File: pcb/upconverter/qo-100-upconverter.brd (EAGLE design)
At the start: 85 x 60 mm, 170 parts, among them CON1 2EDG-2P, Q1 AO3400, Q2 AO3401, U1 EFM32PG1B200F256GM32, U10 MIC23155, U11 LT8636, U12 ADP3334, U13 LT8636, U14 ADP150UJZ-3.3, U15 ADP150UJZ-3.3, U2 DSB321SDA, U3 ADF4351, U4 HMC8073, U5 MAX2671, U6 2450BP15E0100, U7 ADL5601, U8 ADL5601, U9 ADPA9002

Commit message: Lots of changes PCBs in production Stencil in production Added and changed simulation files
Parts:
- added C90: 10uF, Capacitor:CAP1206
- C27: value 10uF -> 100nF
- C28: value 100nF -> 10uF
- C29: value 100pF -> 100nF
- C30: value 47pF -> 100pF
- C32: value 220pF -> 47pF
- C33: value DNP -> 220pF
- C34, C49: value 12pF -> DNP
- C35: value 100uF -> 12pF; device Capacitor:CAP1206 -> Capacitor:CAP0603
- C36: value 1uF -> 100uF; device Capacitor:CAP0603 -> Capacitor:CAP1206
- C37, C41: value 1nF -> 1uF
- C38, C42: value 15pF -> 1nF
- C39, C43: value 12pF -> 15pF
- C40: value 1uF -> 12pF
- C44: value 0 Ohms -> 12pF
- C45: value 12pF -> 0 Ohms
- C46: value 22uF -> 12pF; device Capacitor:CAP1206 -> Capacitor:CAP0603
- C47: value 1nF -> 22uF; device Capacitor:CAP0603 -> Capacitor:CAP1206
- C48: value DNP -> 1nF
- C50: value DNP -> 12pF
- C53: value 1nF -> DNP
- C54: value 100nF -> 1nF
- C55: value 4.7uF -> 100nF
- C57: value 470pF -> 4.7uF
- C58, C60, C78: value 1uF -> 470pF
- C59, C77: value 470pF -> 1uF
- C62, C79: value 10nF -> 1uF
- C63: value 470pF -> 10nF
- C64: value 100nF -> 470pF
- C66, C81: value 10pF -> 100nF
- C67: value 470pF -> 10pF
- C68: value 100uF -> 470pF; device Capacitor:CAP1206 -> Capacitor:CAP0603
- C70: value 100nF -> 100uF; device Capacitor:CAP0603 -> Capacitor:CAP1206
- C71, C76: value 1uF -> 100nF
- C72: value 4.7uF -> 1uF
- C73: value 22uF -> 4.7uF; device Capacitor:CAP1206 -> Capacitor:CAP0603
- C74, C85: value 1uF -> 22uF; device Capacitor:CAP0603 -> Capacitor:CAP1206
- C75: value 100nF -> 1uF
- C80: value 100nF -> 10nF
- C82: value 1uF -> 10pF
- C84, C87: value 22uF -> 1uF; device Capacitor:CAP1206 -> Capacitor:CAP0603
- C88: value 100nF -> 22uF; device Capacitor:CAP0603 -> Capacitor:CAP1206
- C89: value 10uF -> 100nF; device Capacitor:CAP1206 -> Capacitor:CAP0603
- U4: value HMC8073 -> F1951NBGI; device Analog Devices:LFCSP16 -> Renesas:QFN24
- moved C82 42.1 mm to (7.00, 24.7), turned to 0 degrees
- moved C54 37.8 mm to (16.4, 44.5), turned to 270 degrees
- moved C67 31.4 mm to (21.6, 2.50), turned to 0 degrees
- moved C63 29.4 mm to (21.6, 7.90)
- moved C72 28.1 mm to (41.7, 39.1), turned to 270 degrees
- moved C78 27.1 mm to (33.6, 39.1), turned to 270 degrees
- moved C85 25.1 mm to (30.3, 31.5), turned to 0 degrees
- moved C87 24.2 mm to (51.7, 40.1), turned to 270 degrees
- moved C71 22.8 mm to (34.3, 17.5), turned to 90 degrees
- moved C77 22.2 mm to (17.3, 24.1), turned to 0 degrees
- moved C58 22.1 mm to (50.7, 10.6), turned to 180 degrees
- moved C60 21.8 mm to (43.2, 16.2), turned to 90 degrees
- moved C55 20.1 mm to (41.4, 16.2), turned to 90 degrees
- moved C59 19.0 mm to (30.1, 2.50), turned to 0 degrees
- moved C56 18.8 mm to (26.7, 2.50), turned to 180 degrees
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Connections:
- removed net ATT_LE: R10.2, U1.24, U4.12
- new net !ATT_CS: R10.2, U1.24, U4.9
- new net N$28: C27.1, U4.2
- net 12V0: now also C82.1, C85.1, C89.1; no longer C81.1, C84.1, C87.1
- net 12V0_ANA_PA_CLEAN: now also C47.1, C74.1, C76.1; no longer C45.1, C73.1, C75.1
- net 12V0_BST: now also C81.2; no longer C80.2
- net 12V0_FB: now also C82.2; no longer C81.2
- net 12V0_INTVCC: now also C79.1; no longer C78.1
- net 12V0_SS: now also C80.1; no longer C79.1
- net 12V0_SW: now also C81.1; no longer C80.1
- net 12V0_VSENSE: now also C64.1; no longer C63.1
- net 3V3: now also C65.1, C69.1; no longer C64.1, C68.1
- net 3V3_ANA_MIXER_CLEAN: now also C29.1, C32.1, C86.1, U4.14; no longer C27.1, C30.1, C85.1, U4.1
- net 3V3_ANA_PLL_CLEAN: now also C87.1; no longer C86.1
- net 3V3_SOFTSTART: now also C60.1; no longer C59.1
- net 5V0: now also C55.1, C57.1, C67.1, C72.1, C84.1; no longer C54.1, C56.1, C66.1, C69.1, C82.1
- net 5V0_ANA_PA_CLEAN: now also C39.1, C43.1, C78.1; no longer C35.1, C40.1, C77.1
- net 5V0_BST: now also C66.2; no longer C65.2
- net 5V0_FB: now also C67.2; no longer C66.2
- net 5V0_INTVCC: now also C62.1; no longer C61.1
- net 5V0_SS: now also C63.1; no longer C62.1
- net 5V0_SW: now also C66.1; no longer C65.1
- net 5V0_VSENSE: now also C68.1; no longer C67.1
- net GND: now also C32.2, C34.2, C39.2, C43.2, C49.2, C65.2, C77.2, C80.2, C90.2, U4.19, U4.20, U4.21, U4.22, U4.23, U4.24, U4.25; no longer C27.2, C33.2, C35.2, C40.2, C44.2, C50.2, C67.2, C78.2, C82.2, U4.10, U4.11, U4.15, U4.17, U4.2, U4.5, U4.6, U4.7, U4.8
- net N$10: now also C54.1; no longer C53.1
- net N$11: now also C45.1; no longer C44.1
- net N$12: now also C35.2; no longer C34.2
- net N$13: now also C50.1; no longer C49.1
- net N$14: now also C40.1; no longer C39.1
- net N$15: now also C40.2; no longer C39.2
- net N$16: now also C44.1; no longer C43.1
- net N$17: now also C44.2; no longer C43.2
- net N$18: now also C50.2; no longer C49.2
- net N$20: now also C78.2; no longer C77.2
- net N$26: now also U4.17; no longer U4.4
- net N$27: now also C27.2; no longer U4.9
- net N$4: now also C30.1; no longer C29.1
- net N$6: now also C33.1; no longer C32.1
- net N$8: now also C49.1, C51.1; no longer C47.1, C50.1
- net N$9: now also C53.1; no longer C51.1
- net RF_ACC: now also C33.2, C34.1; no longer C32.2, C33.1
- net RF_ACC_FILT: now also C35.1; no longer C34.1
- net SPI_MOSI: now also U4.11; no longer U4.14
- net SPI_SCK: now also U4.8; no longer U4.13
- net VIN: now also C56.1, C59.1, C61.1, C73.1, C75.1, C77.1, C90.1; no longer C55.1, C58.1, C60.1, C72.1, C74.1, C76.1, C89.1
- net VIN_VSENSE: now also C58.1; no longer C57.1
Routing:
- net ATT_LE: track 64.5 -> 0.00 mm, vias 3 -> 0
- net !ATT_CS: track 0.00 -> 60.9 mm, vias 0 -> 3
- net N$27: track 5.45 -> 1.88 mm
- net N$28: track 0.00 -> 1.76 mm
- net SPI_MOSI: track 57.4 -> 56.6 mm
- net 3V3_ANA_MIXER_CLEAN: track 36.7 -> 37.3 mm
- net GND: vias 347 -> 361
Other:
- board text added: "DC IN Max. 24 V"

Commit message: Added LNB controller schematic and PCB Added GPSDO schematic Added example firmware
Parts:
- turned RFCON2 to 270 degrees
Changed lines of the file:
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@@
 <?xml version="1.0" encoding="utf-8"?>
 <!DOCTYPE eagle SYSTEM "eagle.dtd">
-<eagle version="9.5.2">
+<eagle version="9.6.1">
 <drawing>
 <settings>
@@
 <attribute name="NAME" x="83.47" y="45.99" size="0.8" layer="25" font="vector" ratio="10" rot="R180" align="center-left"/>
 </element>
-<element name="RFCON2" library="RF Connector" package="SMA-EDGE" value="RFCON-SMA-EDGE" x="3.5" y="50" smashed="yes" rot="R90">
-<attribute name="NAME" x="5.47" y="45.99" size="0.8" layer="25" font="vector" ratio="10" rot="R180" align="center-left"/>
+<element name="RFCON2" library="RF Connector" package="SMA-EDGE" value="RFCON-SMA-EDGE" x="3.5" y="50" smashed="yes" rot="R270">
+<attribute name="NAME" x="1.53" y="54.01" size="0.8" layer="25" font="vector" ratio="10" align="center-left"/>
 </element>
 <element name="TC1" library="TagConnect" package="TC2050-IDC" value="TC2050-IDC" x="78.1" y="12.3" smashed="yes" rot="R270">

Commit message: Change some component values
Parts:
- C12: value 100nF -> 10pF
- C35, C40, C44, C50: value 12pF -> 15pF
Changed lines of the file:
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@@
 <attribute name="VOLTAGE" value="" x="72.35" y="133.17" size="1.778" layer="27" rot="R90" display="off"/>
 </element>
-<element name="C40" library="Capacitor" package="CAP0603" value="12pF" x="31" y="50.5" smashed="yes" rot="R180">
+<element name="C40" library="Capacitor" package="CAP0603" value="15pF" x="31" y="50.5" smashed="yes" rot="R180">
 <attribute name="NAME" x="29.4536" y="51.916" size="0.8" layer="25" font="vector" ratio="10" rot="SR0" align="center-left"/>
 <attribute name="VALUE" x="33.9464" y="52.532" size="0.8" layer="27" font="vector" ratio="10" rot="SR180" align="center-left"/>
 <attribute name="VOLTAGE" value="" x="0.52" y="122.89" size="1.778" layer="27" rot="R180" display="off"/>
 </element>
-<element name="C35" library="Capacitor" package="CAP0603" value="12pF" x="41" y="50.5" smashed="yes" rot="R180">
+<element name="C35" library="Capacitor" package="CAP0603" value="15pF" x="41" y="50.5" smashed="yes" rot="R180">
 <attribute name="NAME" x="39.5536" y="51.916" size="0.8" layer="25" font="vector" ratio="10" rot="SR0" align="center-left"/>
 <attribute name="VALUE" x="43.9464" y="52.532" size="0.8" layer="27" font="vector" ratio="10" rot="SR180" align="center-left"/>
@@
 <attribute name="VOLTAGE" value="" x="-46.88" y="117.19" size="1.778" layer="27" rot="R180" display="off"/>
 </element>
-<element name="C50" library="Capacitor" package="CAP0603" value="12pF" x="9" y="50" smashed="yes" rot="R180">
+<element name="C50" library="Capacitor" package="CAP0603" value="15pF" x="9" y="50" smashed="yes" rot="R180">
 <attribute name="NAME" x="7.4536" y="51.416" size="0.8" layer="25" font="vector" ratio="10" rot="SR0" align="center-left"/>
 <attribute name="VALUE" x="11.9464" y="52.032" size="0.8" layer="27" font="vector" ratio="10" rot="SR180" align="center-left"/>
 <attribute name="VOLTAGE" value="" x="-51.96" y="122.39" size="1.778" layer="27" rot="R180" display="off"/>
 </element>
-<element name="C44" library="Capacitor" package="CAP0603" value="12pF" x="21" y="50.5" smashed="yes" rot="R180">
+<element name="C44" library="Capacitor" package="CAP0603" value="15pF" x="21" y="50.5" smashed="yes" rot="R180">
 <attribute name="NAME" x="19.4536" y="51.916" size="0.8" layer="25" font="vector" ratio="10" rot="SR0" align="center-left"/>
 <attribute name="VALUE" x="23.9464" y="52.532" size="0.8" layer="27" font="vector" ratio="10" rot="SR180" align="center-left"/>
@@
 <attribute name="VOLTAGE" value="" x="-22.85" y="-49.5" size="1.778" layer="27" rot="R270" display="off"/>
 </element>
-<element name="C12" library="Capacitor" package="CAP0603" value="100nF" x="62.3" y="27.5" smashed="yes" rot="R180">
+<element name="C12" library="Capacitor" package="CAP0603" value="10pF" x="62.3" y="27.5" smashed="yes" rot="R180">
 <attribute name="NAME" x="60.7536" y="28.916" size="0.8" layer="25" font="vector" ratio="10" rot="SR0" align="center-left"/>
 <attribute name="VALUE" x="65.2464" y="29.532" size="0.8" layer="27" font="vector" ratio="10" rot="SR180" align="center-left"/>

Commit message: Finish general filter PCB Fix screw not connected to GND on upconverter PCB Some work on upconverter software
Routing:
- net GND: vias 361 -> 362
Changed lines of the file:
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@@
 <via x="75.2" y="48.9" extent="1-16" drill="0.3"/>
 <via x="74.3" y="49.3" extent="1-16" drill="0.3"/>
+<via x="82" y="3" extent="1-16" drill="3" diameter="5.5" alwaysstop="yes"/>
 </signal>
 <signal name="3V3">
@@
 <wire x1="63.7" y1="50.5" x2="65.58085" y2="50.5" width="0.5" layer="1"/>
 </signal>
-<signal name="GND1">
-<via x="82" y="3" extent="1-16" drill="3" diameter="5.5" alwaysstop="yes"/>
-</signal>
 <signal name="N$28">

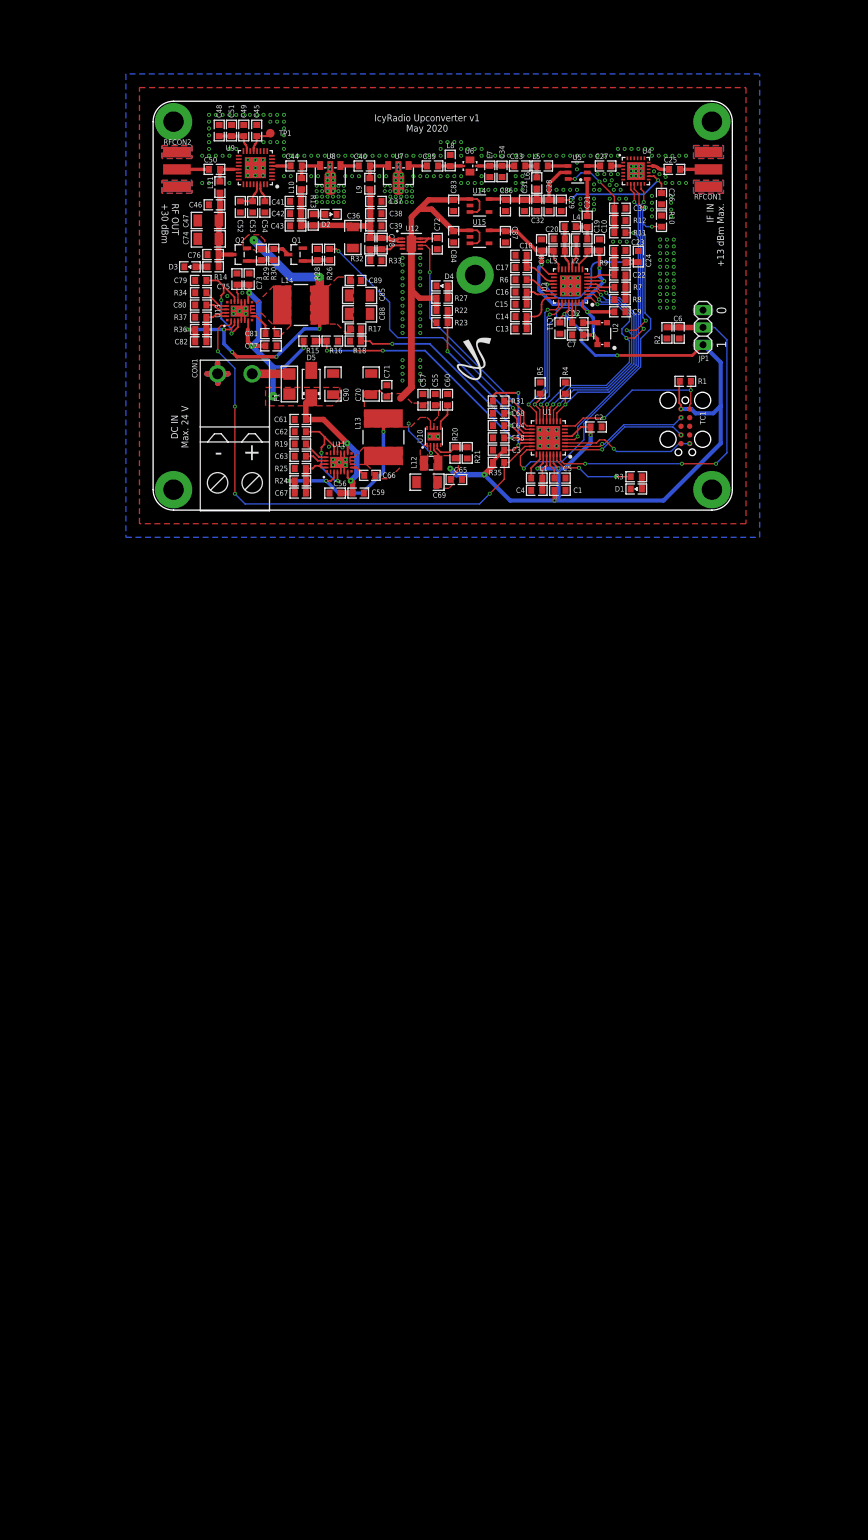
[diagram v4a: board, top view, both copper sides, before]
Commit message: Start upconverter redesign
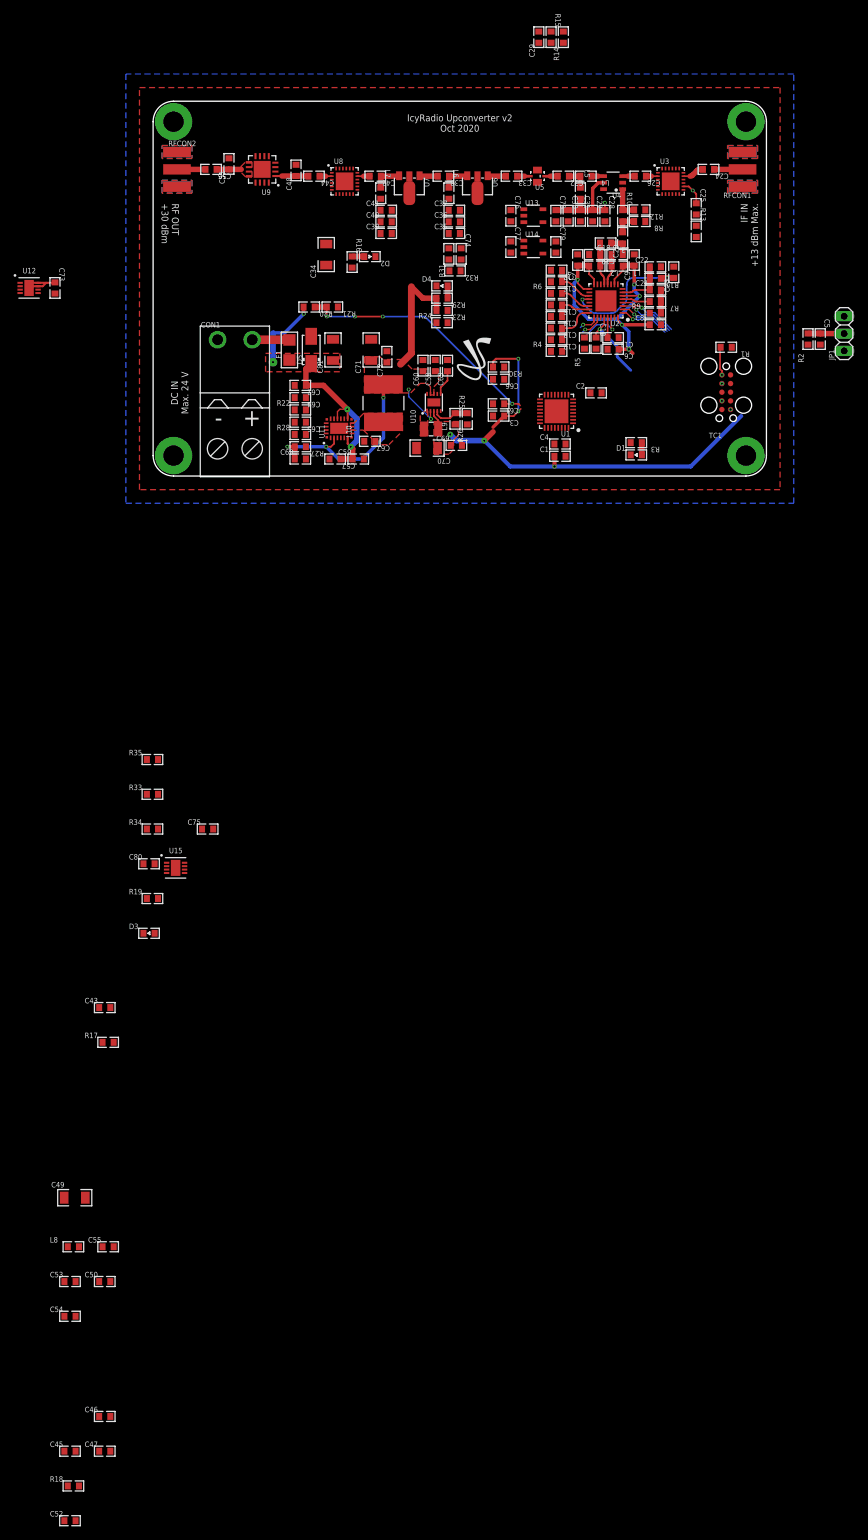
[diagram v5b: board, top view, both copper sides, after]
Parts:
- removed C82: 10pF, Capacitor:CAP0603
- removed C83, C84, C86, C87: 1uF, Capacitor:CAP0603
- removed C85, C88: 22uF, Capacitor:CAP1206
- removed C89: 100nF, Capacitor:CAP0603
- removed C90: 10uF, Capacitor:CAP1206
- removed L11: 47nH, Inductor:IND0603
- removed L12: 2.2uH, Inductor:IND2520
- removed L13, L14: 4.7uH, Inductor:IND0606
- removed Q1: AO3400, Alpha Omega:SOT23
- removed Q2: AO3401, Alpha Omega:SOT23
- removed R36: 1M Ohms, Resistor:RES0603
- removed R37: 86.6K Ohms, Resistor:RES0603
- removed TP1: TESTPOINT-1.27MM, PADs:PAD1.27MM
- C11, C13, C15, C17: value 100nF -> 10pF
- C12, C14, C16, C67: value 10pF -> 100nF
- C18: value 10pF -> 0.7pF
- C20: value 0.7pF -> 15pF
- C21: value 15pF -> 39nF
- C22: value 39nF -> 2.7nF
- C23: value 2.7nF -> 1.2nF
- C24: value 1.2nF -> 100nF
- C26, C28: value 10uF -> 100nF
- C27: value 100nF -> 10uF
- C29: value 100nF -> 100pF
- C30: value 100pF -> 47pF
- C32: value 47pF -> 220pF
- C33: value 220pF -> 15pF
- C34, C49: value DNP -> 100uF; device Capacitor:CAP0603 -> Capacitor:CAP1206
- C35, C39, C50: value 15pF -> 1uF
- C36: value 100uF -> 1nF; device Capacitor:CAP1206 -> Capacitor:CAP0603
- C37, C41: value 1uF -> 15pF
- C38, C42: value 1nF -> 15pF
- C4, C73: value 4.7uF -> 1uF
- C40: value 15pF -> 1nF
- C43: value 15pF -> 100nF
- C45: value 0 Ohms -> 10uF
- C46: value 12pF -> 10nF
- C47: value 22uF -> 100pF; device Capacitor:CAP1206 -> Capacitor:CAP0603
- C48: value 1nF -> 2pF
- C5, C72: value 1uF -> 100nF
- C51: value DNP -> 3.3F
- C52: value DNP -> 100nF
- C53: value DNP -> 10nF
- C54: value 1nF -> 100pF
- C55: value 100nF -> 15pF
- C56: value 4.7uF -> 15pF
- C58: value 470pF -> 100nF
- C60: value 470pF -> 4.7uF
- C61: value 1uF -> 470pF
- C63, C80: value 10nF -> 470pF
- C64, C78: value 470pF -> 1uF
- C65: value 100nF -> 10nF
- C66: value 100nF -> 470pF
- C68: value 470pF -> 10pF
- C69: value 100uF -> 100nF; device Capacitor:CAP1206 -> Capacitor:CAP0603
- C71: value 100nF -> 100uF; device Capacitor:CAP0603 -> Capacitor:CAP1206
- C74: value 22uF -> 470pF; device Capacitor:CAP1206 -> Capacitor:CAP0603
- C76: value 100nF -> 1uF
- C81: value 100nF -> 10uF; device Capacitor:CAP0603 -> Capacitor:CAP1206
- L1: value 4.7uH -> 3.3nH
- L10: value 470nH -> 4.7uH; device Inductor:IND0603 -> Inductor:IND0606
- L2: value 3.3nH -> 10nH
- L3: value 10nH -> 3.3nH
- L5: value 3.3nH -> 1.8nH
- L6: value 1.8nH -> 470nH
- L7: value DNP -> 470nH
- L8: value DNP -> 47nH
- L9: value 470nH -> 2.2uH; device Inductor:IND0603 -> Inductor:IND2520
- R10: value 100K Ohms -> 61.9 Ohms
- R11: value 100 Ohms -> 680 Ohms
- R12: value 100K Ohms -> 105 Ohms
- R13: value 510 Ohms -> 100K Ohms
- R14: value 2K Ohms -> 100 Ohms
- R15, R17: value 147K Ohms -> 100K Ohms
- R16: value 21K Ohms -> 510 Ohms
- R18: value 21K Ohms -> 100 Ohms
- R19: value 41.2K Ohms -> 510 Ohms
- R20: value 309K Ohms -> 147K Ohms
- R21: value 71.5K Ohms -> 21K Ohms
- R22: value 100K Ohms -> 41.2K Ohms
- R24: value 1M Ohms -> 100K Ohms
- R25: value 226K Ohms -> 309K Ohms
- R26: value 22 Ohms -> 71.5K Ohms
- R27: value 510 Ohms -> 1M Ohms
- R28: value 10K Ohms -> 226K Ohms
- R29: value 10K Ohms -> 510 Ohms
- R30: value 3.9K Ohms -> 100K Ohms
- R31: value 100K Ohms -> 210K Ohms
- R32: value 210K Ohms -> 64.9K Ohms
- R33: value 64.9K Ohms -> 100K Ohms
- R34: value 41.2K Ohms -> 210K Ohms
- R35: value 100K Ohms -> 64.9K Ohms
- R8: value 360 Ohms -> 105 Ohms
- R9: value 680 Ohms -> 360 Ohms
- U1: value EFM32PG1B200F256GM32 -> EFM32PG1B100F256GM32
- U13: value LT8636 -> ADP7142AUJZ-3.3; device Analog Devices:QFN20_ASYM_CORNER -> Analog Devices:SOT23-5
- U14: value ADP150UJZ-3.3 -> ADP7142AUJZ-3.3
- U15: value ADP150UJZ-3.3 -> ADP3334; device Analog Devices:SOT23-5 -> Analog Devices:LFCSP8_3X3
- U2: value DSB321SDA -> ADF4351; device Crystal:TCXO-3225 -> Analog Devices:QFN32
- U3: value ADF4351 -> F1951NBGI; device Analog Devices:QFN32 -> Renesas:QFN24
- U4: value F1951NBGI -> MAX2671; device Renesas:QFN24 -> Maxim Integrated:SOT23-6
- U5: value MAX2671 -> 2450BP15E0100; device Maxim Integrated:SOT23-6 -> Generic Filter:2450BP15E0100
- U6: value 2450BP15E0100 -> ADL5601; device Generic Filter:2450BP15E0100 -> Analog Devices:SOT89
- U8: value ADL5601 -> F1951NBGI; device Analog Devices:SOT89 -> Renesas:QFN24
- U9: value ADPA9002 -> ADL5606; device Analog Devices:QFN32 -> Analog Devices:LFCSP16_4X4
- moved C45 195.7 mm to (-12.2, -138.1), turned to 0 degrees
- moved C52 194.4 mm to (-12.2, -148.3), turned to 0 degrees
- moved C47 181.2 mm to (-7.10, -138.1), turned to 0 degrees
- moved C46 178.5 mm to (-7.10, -133.0), turned to 0 degrees
- moved R18 173.0 mm to (-11.7, -143.2)
- moved L8 168.7 mm to (-11.7, -108.1), turned to 0 degrees
- moved C54 165.3 mm to (-12.2, -118.3), turned to 0 degrees
- moved C50 164.0 mm to (-7.10, -113.2), turned to 0 degrees
- moved C53 160.0 mm to (-12.2, -113.2), turned to 0 degrees
- moved C49 158.6 mm to (-11.5, -100.9), turned to 0 degrees
- moved C55 133.2 mm to (-6.60, -108.1), turned to 0 degrees
- moved C43 118.1 mm to (-7.10, -73.0), turned to 0 degrees
- moved R17 110.8 mm to (-6.60, -78.1), turned to 0 degrees
- moved U15 102.8 mm to (3.30, -52.5)
- moved D3 98.0 mm to (-0.60, -62.1)
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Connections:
- removed net !5V0_PA_BIAS_EN: R31.1, U1.17, U12.6
- removed net !ATT_CS: R10.2, U1.24, U4.9
- removed net 12V0: C82.1, C85.1, C88.1, C89.1, L14.2, Q2.2, R17.2, R29.2, R36.2, U13.2
- removed net 12V0_ANA_PA_CLEAN: C46.1, C47.1, C74.1, C76.1, L11.2, Q2.3, R14.2
- removed net 12V0_BST: C81.2, U13.7
- removed net 12V0_FB: C82.2, R36.1, R37.2, U13.19, U13.20
- removed net 12V0_INTVCC: C79.1, U13.15, U13.3
- removed net 12V0_PA_BIAS_EN: R26.2, U1.18
- removed net 12V0_PGOOD: R35.1, U1.23, U13.1
- removed net 12V0_RT: R34.2, U13.17
- removed net 12V0_SS: C80.1, U13.18
- removed net 12V0_SW: C81.1, L14.1, U13.10, U13.8, U13.9
- removed net 12V0_VSENSE: C64.1, R17.1, R18.2, U1.20
- removed net 1V8: C4.1, L1.1, U1.28
- removed net 3V3_ANA_MIXER_CLEAN: C26.1, C28.1, C29.1, C31.1, C32.1, C86.1, L6.2, U14.5, U4.14, U5.5
- removed net 5V0_ANA_PA_CLEAN: C36.1, C37.1, C38.1, C39.1, C41.1, C42.1, C43.1, C78.1, L10.2, L9.2, R13.2, R32.2, U12.1, U12.2
- removed net N$11: C45.1, TP1.TP, U9.13
- removed net N$13: C50.1, L11.1, U9.21
- removed net N$17: C44.2, U9.5
- removed net N$21: L1.2, U1.26
- removed net N$24: D3.A, R14.1
- new net !IF_ATT_CS: U1.24, U3.9
- new net !IF_ATT_RST: R13.2, U3.7
- new net !PA_BIAS_EN: R30.1, R33.1, U1.17, U12.6, U15.6
- new net !RF_ATT_CS: U8.9
- new net !RF_ATT_RST: R17.2, U8.7
- new net 3V3_ANA_MIXER_ATT_CLEAN: C25.1, C27.1, C28.1, C30.1, C31.1, C43.1, C78.1, L5.2, U13.4, U13.5, U3.14, U4.5, U8.14
- new net 5V0_PA_STG1_CLEAN: C34.1, C35.1, C36.1, C37.1, C39.1, C40.1, C41.1, C74.1, L6.2, L7.2, R16.2, R31.2, U12.1, U12.2
- new net 5V0_PA_STG2_CLEAN: C45.1, C46.1, C47.1, C49.1, C50.1, C53.1, C54.1, C55.1, C80.1, L8.2, R19.2, R34.2, U15.1, U15.2, U9.3, U9.4
- new net N$29: C20.2, R10.2, R8.2
- new net PA_DISABLE: R18.1
- new net RF_ACC_PRE: C42.2, U8.17
- net !MIXER_SHDN: now also R14.2; no longer R11.2
- net !PLL_MUTE: now also U2.26; no longer U3.26
- net !RESET: now also U1.9; no longer U1.8
- net 3V3: now also C10.1, C70.1, L9.2, R25.2, R30.2, R33.2, U1.25, U1.6, U2.28; no longer C11.1, C65.1, L12.2, R20.2, R31.2, R35.2, U1.30, U1.5, U3.28
- net 3V3_ANA_PLL_CLEAN: now also C6.1, C79.1, L1.1, L2.2, U14.4, U14.5, U2.10, U2.16, U2.17, U2.32, U2.6; no longer C10.1, C87.1, L2.1, L3.2, U15.5, U2.4, U3.10, U3.16, U3.17, U3.32, U3.6
- net 3V3_FB: now also R25.1, R26.2; no longer R20.1, R21.2
- net 3V3_SOFTSTART: now also C63.1; no longer C60.1
- net 3V3_SW: now also L9.1; no longer L12.1
- net 5V0: now also C58.1, C60.1, C68.1, C73.1, C75.1, C76.1, C77.1, L10.2, R23.2, R29.2, U13.1, U13.3, U15.7, U15.8, U15.9; no longer C55.1, C57.1, C67.1, C70.1, C83.1, C84.1, L13.2, R22.2, R24.2, U15.1, U15.3
- net 5V0_BST: now also C67.2; no longer C66.2
- net 5V0_FB: now also C68.2, R27.1, R28.2; no longer C67.2, R24.1, R25.2
- net 5V0_INTVCC: now also C64.1; no longer C62.1
- net 5V0_RT: now also R22.2; no longer R19.2
- net 5V0_SS: now also C65.1; no longer C63.1
- net 5V0_SW: now also C67.1, L10.1; no longer C66.1, L13.1
- net 5V0_VSENSE: now also C66.1, R23.1, R24.2; no longer C68.1, R22.1, R23.2
- net GND: now also C12.2, C19.2, C22.2, C25.2, C27.2, C35.2, C40.2, C50.2, C66.2, C78.2, C81.2, R13.1, R15.1, R17.1, R22.1, R24.1, R26.1, R32.1, R35.1, R9.1, U13.2, U15.5, U2.11, U2.18, U2.21, U2.27, U2.31, U2.33, U2.8, U2.9, U3.16, U3.19, U3.20, U3.22, U3.23, U3.24, U3.25, U3.3, U4.2, U5.1, U5.3, U6.2, U6.4, U8.16, U8.19, U8.20, U8.21, U8.22, U8.23, U8.24, U8.25, U8.3; no longer C11.2, C18.2, C20.2, C24.2, C26.2, C32.2, C38.2, C42.2, C56.2, C68.2, C74.2, C80.2, C83.2, C84.2, C85.2, C86.2, C87.2, C88.2, C89.2, C90.2, L7.2, L8.2, Q1.2, R10.1, R16.1, R18.1, R19.1, R23.1, R25.1, R33.1, R34.1, R37.1, U1.25, U13.12, U13.13, U13.21, U13.4, U13.5, U13.M1, U13.M2, U13.M3, U13.M4, U15.2, U2.1, U2.2, U3.11, U3.18, U3.27, U3.31, U3.33, U3.8, U3.9, U4.16, U4.19, U4.20, U4.21, U4.22, U4.23, U4.24, U4.25, U4.3, U5.2, U6.1, U6.3, U8.2, U8.4, U9.1, U9.16, U9.20, U9.22, U9.24, U9.25, U9.32, U9.33, U9.4, U9.6, U9.8, U9.9
- net IF_FREQ_SEL: now also C5.1; no longer C6.1
- net IF_IN_DCC: now also C24.1; no longer C25.1
- net MIXER_LO: now also R10.1, R12.2, U4.1; no longer C21.2, U5.1
- net N$1: now also C18.2, C20.1, L3.1; no longer C19.2, C21.1, L4.1
- net N$10: now also C52.1, R18.2, U9.2; no longer C54.1, U9.30
- net N$12: now also C33.2, U6.1; no longer C35.2, U7.1
- net N$14: now also C38.1, L6.1, U6.3; no longer C40.1, L9.1, U7.3
- net N$149: now also R29.1; no longer R27.1
- net N$15: now also C38.2, U7.1; no longer C40.2, U8.1
- net N$16: now also C42.1, L7.1, U7.3; no longer C44.1, L10.1, U8.3
- net N$18: now also C56.2; no longer C50.2
- net N$2: now also C80.2, R34.1, R35.2, U15.3; no longer Q1.1, R26.1, R28.2
- net N$20: now also C74.2, R31.1, R32.2; no longer C78.2, R32.1, R33.2
- net N$22: now also C4.1, U1.26; no longer C5.1, U1.29
- net N$23: now also R16.1; no longer R13.1
- net N$26: now also C24.2, U3.17; no longer C25.2, U4.17
- net N$27: now also C26.2, U4.3; no longer C27.2, U5.3
- net N$28: now also C26.1, U3.2; no longer C27.1, U4.2
- net N$3: now also D3.A, R19.1; no longer Q2.1, R29.1, R30.2
- net N$4: now also C29.1, R14.1, R15.2, U4.6; no longer C30.1, R11.1, R12.2, U5.6
- net N$5: now also C44.2, C48.1, U9.1; no longer Q1.3, R30.1
- net N$6: now also C32.1, L4.2, L5.1; no longer C33.1, L5.2, L6.1
- net N$67: now also C19.1, L2.1, L3.2, U2.13; no longer C20.1, L3.1, L4.2, U3.13
- net N$69: now also C18.1, L1.2, U2.12; no longer C19.1, L2.2, U3.12
- net N$7: now also L4.1, U4.4; no longer L5.1, U5.4
- net N$8: now also C56.1, L8.1, U9.10, U9.11, U9.12, U9.9; no longer C48.1, C49.1, U9.15
- net N$84: now also C21.2, R9.2; no longer C22.2, R8.2
- net N$88: now also U2.22; no longer U3.22
- net N$9: now also C44.1, U8.2; no longer C52.1, C53.1, U9.29
- net PLL_CP_VOUT: now also C21.1, R11.2, U2.7; no longer C23.1, R9.2, U3.7
- net PLL_EN: now also U2.4; no longer U3.4
- net PLL_FASTLOCK_SW: now also U2.5; no longer U3.5
- net PLL_LE: now also U2.3; no longer U3.3
- net PLL_LOCK: now also U2.25; no longer U3.25
- net PLL_MUXOUT: now also U2.30; no longer U3.30
- net PLL_REF_ACC: now also C11.2, U2.29; no longer C12.2, U3.29
- net PLL_REF_DCC: now also C11.1; no longer C12.1, U2.3
- net PLL_TEMP: now also C16.1, U2.19; no longer C18.1, U3.19
- net PLL_VCOM: now also C14.1, U2.23; no longer C16.1, U3.23
- net PLL_VREF: now also C12.1, U2.24; no longer C14.1, U3.24
- net PLL_VTUNE: now also C23.1, R11.1, U2.20; no longer C24.1, R9.1, U3.20
- net RF_ACC: now also C32.2, U5.4; no longer C33.2, C34.1, L7.1, U6.4
- net RF_ACC_FILT: now also C33.1, U5.2; no longer C35.1, L8.1, U6.2
- net SPI_MOSI: now also U2.2, U3.11, U8.11; no longer U3.2, U4.11
- net SPI_SCK: now also U2.1, U3.8, U8.8; no longer U3.1, U4.8
- net VIN: now also C57.1, C62.1, C81.1, R20.2; no longer C56.1, C61.1, C73.1, C75.1, C77.1, C90.1, R15.2, U13.11, U13.14, U13.6
- net VIN_VSENSE: now also C61.1, R20.1, R21.2; no longer C58.1, R15.1, R16.2
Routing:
- net 12V0_PGOOD: track 77.1 -> 0.00 mm, vias 4 -> 0
- net 3V3: track 151.1 -> 87.1 mm, vias 11 -> 7
- net !ATT_CS: track 60.9 -> 0.00 mm, vias 3 -> 0
- net SPI_SCK: track 57.2 -> 7.40 mm, vias 5 -> 1
- net 12V0: track 48.9 -> 0.00 mm, vias 7 -> 0
- net SPI_MOSI: track 56.6 -> 7.87 mm, vias 5 -> 1
- net IF_FREQ_SEL: track 52.3 -> 5.31 mm, vias 3 -> 0
- net 12V0_PA_BIAS_EN: track 43.7 -> 0.00 mm, vias 2 -> 0
- net 5V0: track 103.2 -> 61.1 mm
- net 3V3_ANA_MIXER_CLEAN: track 37.3 -> 0.00 mm, vias 2 -> 0
- net !MIXER_SHDN: track 37.1 -> 0.00 mm, vias 2 -> 0
- net !5V0_PA_BIAS_EN: track 35.5 -> 0.00 mm, vias 2 -> 0
- net 12V0_VSENSE: track 33.8 -> 0.00 mm, vias 2 -> 0
- net 5V0_ANA_PA_CLEAN: track 29.0 -> 0.00 mm
- net VIN: track 63.8 -> 37.7 mm, vias 6 -> 4
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- added copper zone on layer 1, net N$8
- removed copper zone on layer 1, net 12V0
- removed copper zone on layer 1, net 12V0_SW
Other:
- board size 85 x 60 mm -> 90 x 55 mm
- board text added: "IcyRadio Upconverter v2 Oct 2020"
- board text removed: "0"
- board text removed: "1"
- board text removed: "IcyRadio Upconverter v1 May 2020"
